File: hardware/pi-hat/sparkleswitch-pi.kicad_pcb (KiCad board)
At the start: 2 copper layers, 65 x 56 mm, 21 parts, among them J1 Conn_01x02, J2 Conn_02x06_Odd_Even, P1 CONN_02X20, U1 74HCT245, U2 74HCT245, U3 74HCT245, U4 PC817, U5 PC817, U6 PC817, U7 PC817

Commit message: First version with all connections.
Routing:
- net VCC: track 2.54 -> 118.8 mm, vias 0 -> 2
- net GND: track 82.3 -> 96.0 mm, vias 0 -> 6
- net Net-(R4-Pad2): track 0.00 -> 2.56 mm
- net Net-(R5-Pad1): track 0.00 -> 2.56 mm
- net Net-(R2-Pad2): track 0.00 -> 2.55 mm
- net Net-(R3-Pad2): track 0.00 -> 2.46 mm
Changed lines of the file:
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@@
     (thickness 1.6)
     (drawings 11)
-    (tracks 351)
+    (tracks 424)
     (zones 0)
     (modules 21)
@@
     (46 B.CrtYd user)
     (47 F.CrtYd user)
+    (48 B.Fab user)
+    (49 F.Fab user)
   )
   (setup
-    (last_trace_width 0.2)
+    (last_trace_width 0.5)
     (user_trace_width 0.5)
     (trace_clearance 0.2)
@@
   (segment (start 232.635 118.906) (end 232.635 119.206) (width 0.2) (layer F.Cu) (net 1))
   (segment (start 248.768 123.33) (end 248.768 120.79) (width 0.5) (layer B.Cu) (net 1))
-  (segment (start 248.768 113.272) (end 247.65 112.154) (width 0.5) (layer B.Cu) (net 1))
-  (segment (start 248.768 120.79) (end 248.768 113.272) (width 0.5) (layer B.Cu) (net 1))
   (segment (start 219.379999 97.920001) (end 218.53 98.77) (width 0.2) (layer F.Cu) (net 1))
   (segment (start 219.919999 97.380001) (end 219.379999 97.920001) (width 0.2) (layer F.Cu) (net 1))
   (segment (start 222.459999 97.380001) (end 219.919999 97.380001) (width 0.2) (layer F.Cu) (net 1))
   (segment (start 223.61 96.23) (end 222.459999 97.380001) (width 0.2) (layer F.Cu) (net 1))
+  (segment (start 232.635 118.906) (end 232.635 119.606) (width 0.2) (layer F.Cu) (net 1))
+  (segment (start 235.889 122.06) (end 235.889 122.06) (width 0.2) (layer F.Cu) (net 2))
+  (segment (start 221.205 118.906) (end 221.205 119.606) (width 0.2) (layer F.Cu) (net 1))
+  (segment (start 207.235 118.906) (end 207.235 119.606) (width 0.2) (layer F.Cu) (net 1))
+  (via (at 233.401 120.536) (size 0.9) (drill 0.6) (layers F.Cu B.Cu) (net 1))
+  (via (at 222.098 120.536) (size 0.9) (drill 0.6) (layers F.Cu B.Cu) (net 1))
+  (via (at 208.128 120.663) (size 0.9) (drill 0.6) (layers F.Cu B.Cu) (net 1))
+  (via (at 211.938 123.076) (size 0.9) (drill 0.6) (layers F.Cu B.Cu) (net 1))
+  (via (at 225.908 123.203) (size 0.9) (drill 0.6) (layers F.Cu B.Cu) (net 1))
+  (via (at 237.211 123.203) (size 0.9) (drill 0.6) (layers F.Cu B.Cu) (net 1))
+  (segment (start 232.635 119.77) (end 232.635 118.906) (width 0.2) (layer F.Cu) (net 1))
+  (segment (start 233.401 120.536) (end 232.635 119.77) (width 0.2) (layer F.Cu) (net 1))
+  (segment (start 237.835 123.827) (end 237.835 124.706) (width 0.2) (layer F.Cu) (net 1))
+  (segment (start 237.211 123.203) (end 237.835 123.827) (width 0.2) (layer F.Cu) (net 1))
+  (segment (start 226.405 123.573) (end 226.405 124.706) (width 0.2) (layer F.Cu) (net 1))
+  (segment (start 225.908 123.076) (end 226.405 123.573) (width 0.2) (layer F.Cu) (net 1))
+  (segment (start 221.205 119.643) (end 221.205 118.906) (width 0.2) (layer F.Cu) (net 1))
+  (segment (start 222.098 120.536) (end 221.205 119.643) (width 0.2) (layer F.Cu) (net 1))
+  (segment (start 207.235 119.77) (end 207.235 118.906) (width 0.2) (layer F.Cu) (net 1))
+  (segment (start 208.128 120.663) (end 207.235 119.77) (width 0.2) (layer F.Cu) (net 1))
+  (segment (start 212.435 123.573) (end 212.435 124.706) (width 0.2) (layer F.Cu) (net 1))
+  (segment (start 211.938 123.076) (end 212.435 123.573) (width 0.2) (layer F.Cu) (net 1))
+  (segment (start 247.65 113.28537) (end 247.625 113.31037) (width 0.5) (layer B.Cu) (net 1))
+  (segment (start 247.65 112.154) (end 247.65 113.28537) (width 0.5) (layer B.Cu) (net 1))
+  (segment (start 247.625 119.647) (end 248.768 120.79) (width 0.5) (layer B.Cu) (net 1))
+  (segment (start 247.625 113.31037) (end 247.625 119.647) (width 0.5) (layer B.Cu) (net 1))
   (segment (start 258.928 120.79) (end 258.928 123.33) (width 0.5) (layer B.Cu) (net 2))
+  (segment (start 238.485 118.906) (end 238.485 119.906) (width 0.5) (layer F.Cu) (net 2))
+  (segment (start 230.228 122.187) (end 227.055 122.187) (width 0.5) (layer F.Cu) (net 2))
+  (segment (start 230.24 122.175) (end 230.228 122.187) (width 0.5) (layer F.Cu) (net 2))
+  (segment (start 231.115 122.175) (end 230.24 122.175) (width 0.5) (layer F.Cu) (net 2))
+  (segment (start 227.055 118.906) (end 227.055 122.187) (width 0.5) (layer F.Cu) (net 2))
+  (segment (start 227.055 122.187) (end 227.055 124.706) (width 0.5) (layer F.Cu) (net 2))
+  (segment (start 231.115 122.175) (end 238.37 122.175) (width 0.5) (layer F.Cu) (net 2))
+  (segment (start 238.37 122.175) (end 238.485 122.06) (width 0.5) (layer F.Cu) (net 2))
+  (segment (start 220.179 122.175) (end 220.191 122.187) (width 0.5) (layer F.Cu) (net 2))
+  (segment (start 220.191 122.187) (end 227.055 122.187) (width 0.5) (layer F.Cu) (net 2))
+  (segment (start 219.304 122.175) (end 220.179 122.175) (width 0.5) (layer F.Cu) (net 2))
+  (segment (start 213.097 122.175) (end 213.085 122.187) (width 0.5) (layer F.Cu) (net 2))
+  (segment (start 219.304 122.175) (end 213.097 122.175) (width 0.5) (layer F.Cu) (net 2))
+  (segment (start 213.085 118.906) (end 213.085 122.187) (width 0.5) (layer F.Cu) (net 2))
+  (segment (start 213.085 122.187) (end 213.085 124.706) (width 0.5) (layer F.Cu) (net 2))
+  (segment (start 213.073 122.175) (end 205.334 122.175) (width 0.5) (layer F.Cu) (net 2))
+  (segment (start 213.085 122.187) (end 213.073 122.175) (width 0.5) (layer F.Cu) (net 2))
+  (segment (start 258.928 123.33) (end 257.15 125.108) (width 0.5) (layer B.Cu) (net 2))
+  (via (at 241.91 123.076) (size 0.9) (drill 0.6) (layers F.Cu B.Cu) (net 2))
+  (segment (start 257.15 125.108) (end 243.942 125.108) (width 0.5) (layer B.Cu) (net 2))
+  (segment (start 243.942 125.108) (end 241.91 123.076) (width 0.5) (layer B.Cu) (net 2))
+  (segment (start 241.460001 122.626001) (end 238.543001 122.626001) (width 0.5) (layer F.Cu) (net 2))
+  (segment (start 238.543001 122.626001) (end 238.485 122.568) (width 0.5) (layer F.Cu) (net 2))
+  (segment (start 238.485 122.06) (end 238.485 122.568) (width 0.5) (layer F.Cu) (net 2))
+  (segment (start 241.91 123.076) (end 241.460001 122.626001) (width 0.5) (layer F.Cu) (net 2))
+  (segment (start 238.485 122.568) (end 238.485 124.706) (width 0.5) (layer F.Cu) (net 2))
+  (via (at 241.91 121.552) (size 0.9) (drill 0.6) (layers F.Cu B.Cu) (net 2))
+  (segment (start 241.656 121.298) (end 241.91 121.552) (width 0.5) (layer F.Cu) (net 2))
+  (segment (start 238.485 119.906) (end 238.485 121.298) (width 0.5) (layer F.Cu) (net 2))
+  (segment (start 238.485 121.298) (end 241.656 121.298) (width 0.5) (layer F.Cu) (net 2))
+  (segment (start 238.485 121.298) (end 238.485 122.06) (width 0.5) (layer F.Cu) (net 2))
+  (segment (start 241.91 121.552) (end 241.91 123.076) (width 0.5) (layer B.Cu) (net 2))
+  (segment (start 203.937 100.663) (end 203.937 109.289) (width 0.5) (layer B.Cu) (net 2))
+  (segment (start 208.37 96.23) (end 203.937 100.663) (width 0.5) (layer B.Cu) (net 2))
+  (segment (start 210.91 96.23) (end 208.37 96.23) (width 0.5) (layer B.Cu) (net 2))
+  (segment (start 205.286 107.94) (end 203.937 109.289) (width 0.5) (layer F.Cu) (net 2))
+  (segment (start 205.286 105.042) (end 205.286 107.94) (width 0.5) (layer F.Cu) (net 2))
+  (segment (start 203.937 109.289) (end 202.159 111.067) (width 0.5) (layer F.Cu) (net 2))
+  (segment (start 202.159 111.067) (end 202.159 121.044) (width 0.5) (layer F.Cu) (net 2))
+  (segment (start 203.29 122.175) (end 205.334 122.175) (width 0.5) (layer F.Cu) (net 2))
+  (segment (start 202.159 121.044) (end 203.29 122.175) (width 0.5) (layer F.Cu) (net 2))
   (segment (start 207.288 98.77) (end 205.08 100.978) (width 0.5) (layer F.Cu) (net 3))
   (segment (start 208.37 98.77) (end 207.288 98.77) (width 0.5) (layer F.Cu) (net 3))
@@
   (segment (start 224.455 125.9886) (end 235.7664 137.3) (width 0.2) (layer F.Cu) (net 46))
   (segment (start 224.455 124.706) (end 224.455 125.9886) (width 0.2) (layer F.Cu) (net 46))
+  (segment (start 245.72 112.764) (end 245.11 112.154) (width 0.2) (layer F.Cu) (net 47))
+  (segment (start 245.72 114.452) (end 245.72 112.764) (width 0.2) (layer F.Cu) (net 47))
+  (segment (start 250.546 112.51) (end 250.19 112.154) (width 0.2) (layer F.Cu) (net 48))
+  (segment (start 250.546 114.464) (end 250.546 112.51) (width 0.2) (layer F.Cu) (net 48))
+  (segment (start 255.88 112.764) (end 255.27 112.154) (width 0.2) (layer F.Cu) (net 49))
+  (segment (start 255.88 114.464) (end 255.88 112.764) (width 0.2) (layer F.Cu) (net 49))
+  (segment (start 260.96 112.764) (end 260.35 112.154) (width 0.2) (layer F.Cu) (net 50))
+  (segment (start 260.96 114.464) (end 260.96 112.764) (width 0.2) (layer F.Cu) (net 50))
   (segment (start 246.47 115.952) (end 251.308 120.79) (width 0.2) (layer F.Cu) (net 51))
   (segment (start 245.72 115.952) (end 246.47 115.952) (width 0.2) (layer F.Cu) (net 51))

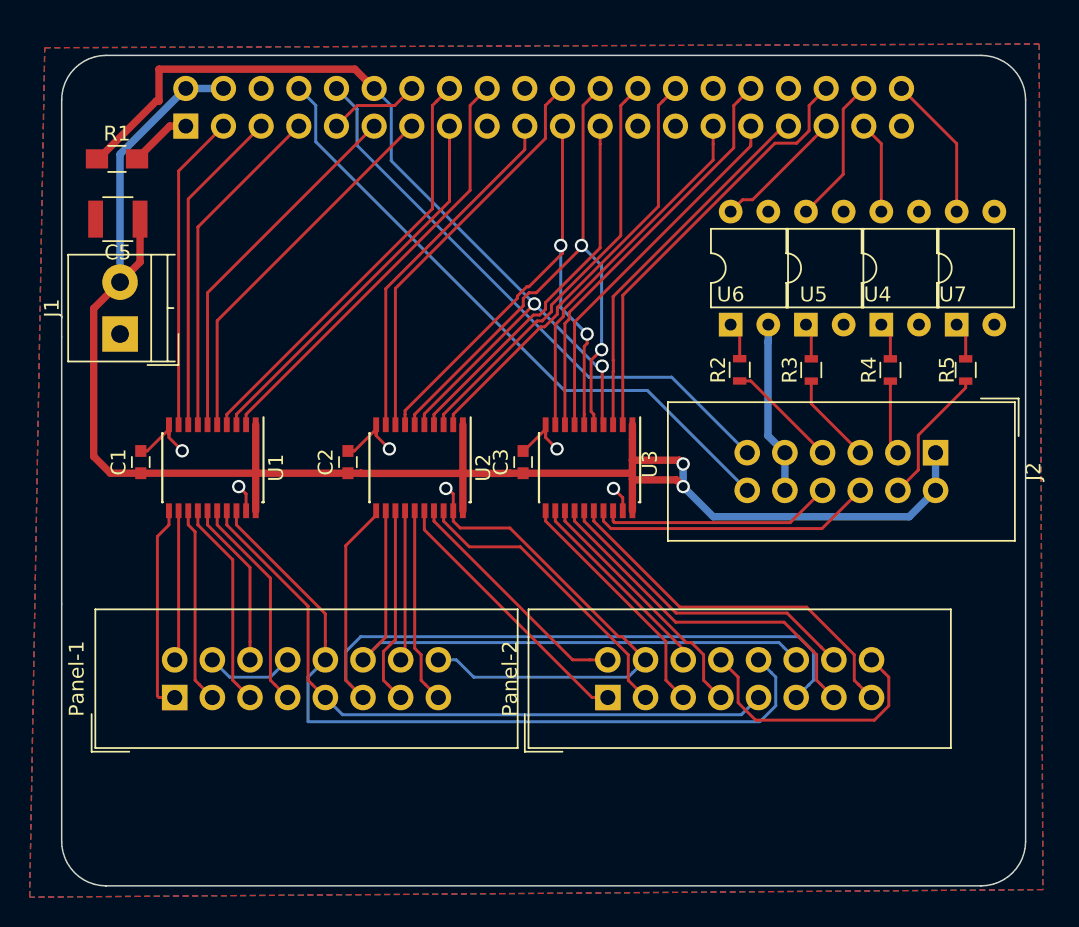
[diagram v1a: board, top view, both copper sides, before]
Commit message: Make traces thicker as we have the space.
o Increase size of traces from 0.25mm to 0.4mm as space is
  not that constricted (right now only the afferent traces).
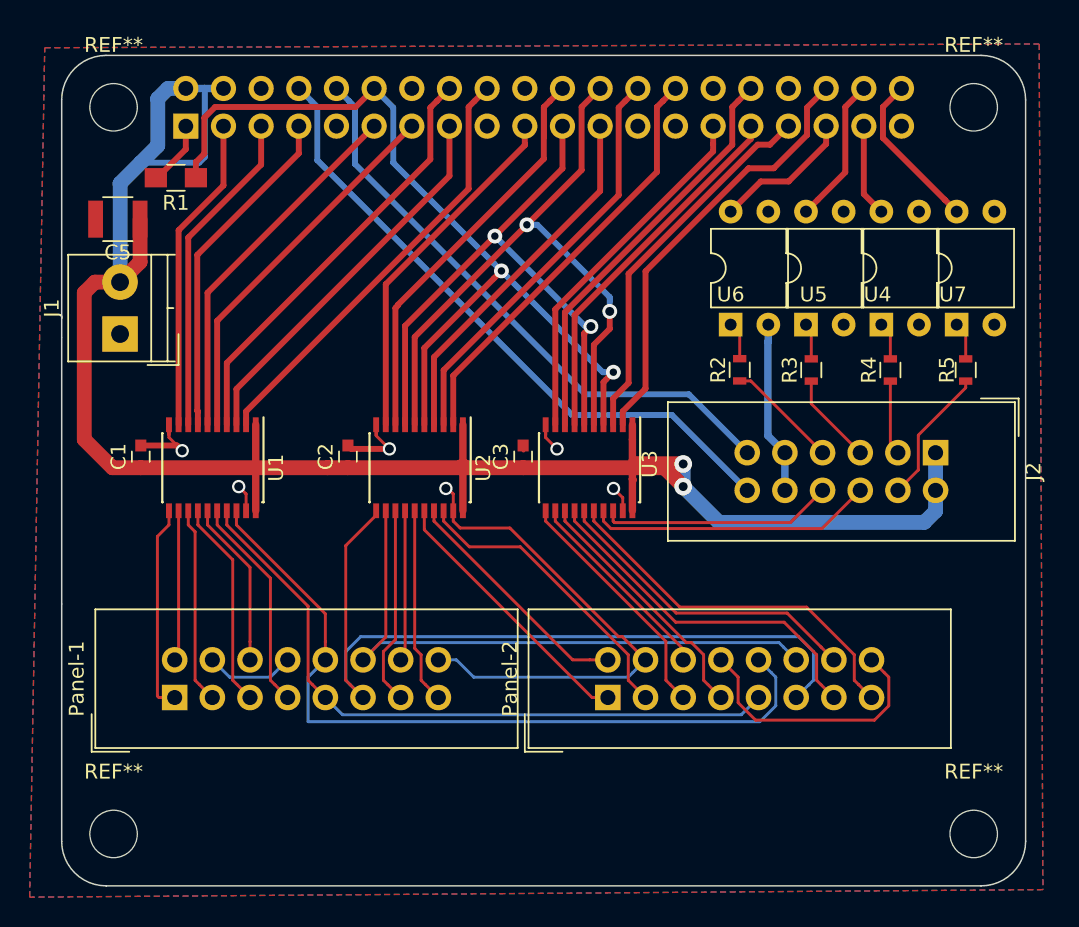
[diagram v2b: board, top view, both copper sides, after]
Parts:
- added REF**: M1, Mounting_Holes:MountingHole_3.2mm_M3, F.Cu at (203.5, 97.5)
- added REF**: M2, Mounting_Holes:MountingHole_3.2mm_M3, F.Cu at (261.5, 97.5)
- added REF**: M3, Mounting_Holes:MountingHole_3.2mm_M3, F.Cu at (261.5, 146.5)
- added REF**: M4, Mounting_Holes:MountingHole_3.2mm_M3, F.Cu at (203.5, 146.5)
- moved R1 4.17 mm to (207.7, 102.2), turned to 180 degrees
- moved C1 0.37 mm to (205.3, 121.1)
- moved C2 0.37 mm to (219.3, 121.1)
- moved C3 0.37 mm to (231.1, 121.1)
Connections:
- P1 pad 9: GND -> Net-(P1-Pad9)
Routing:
- net VCC: track 118.8 -> 135.5 mm
- net GND: track 96.0 -> 88.6 mm
- net OE: track 63.5 -> 60.0 mm
- net strobe: track 41.3 -> 44.5 mm
- net row_D: track 27.3 -> 30.0 mm
- net clock: track 38.1 -> 40.3 mm
- net SenseRelay: track 9.84 -> 10.9 mm
- net RxD: track 39.3 -> 40.1 mm
- net But-On: track 8.83 -> 9.53 mm
- net p0_b2: track 28.9 -> 29.6 mm
- net TxD: track 42.9 -> 43.6 mm
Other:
- net class Default: via_dia 0.9 -> 1

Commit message: Thicker efferent traces.
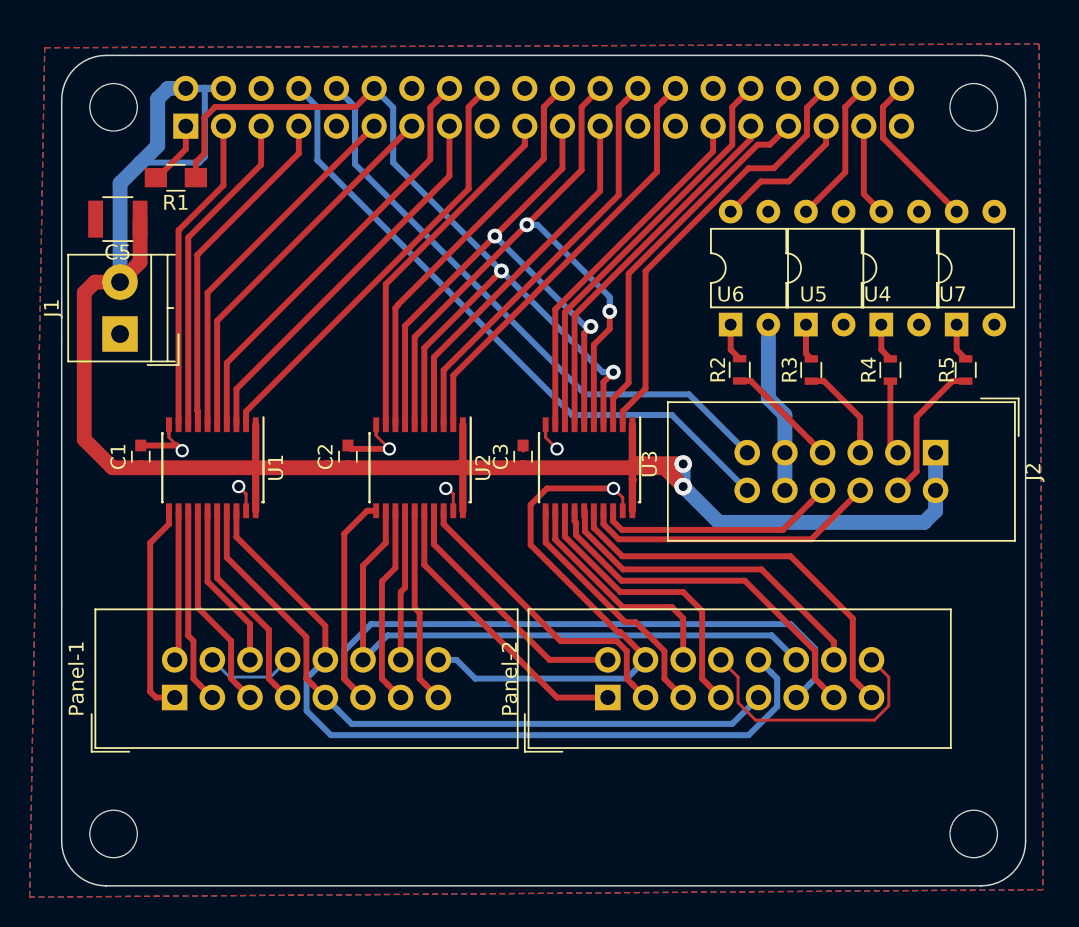
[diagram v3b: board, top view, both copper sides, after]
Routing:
- net GND: track 88.6 -> 90.9 mm
- net p1_b2_buff: track 17.2 -> 19.4 mm
- net p1_g2_buf: track 13.6 -> 15.6 mm
- net OE_buff_1: track 25.4 -> 27.0 mm
- net row_C_buff: track 53.5 -> 55.0 mm
- net p1_r1_buff: track 18.3 -> 19.7 mm
- net strobe_buff_1: track 21.4 -> 22.5 mm
- net p1_g1_buff: track 16.3 -> 17.2 mm
- net row_B_buff: track 52.5 -> 53.4 mm
- net Net-(R4-Pad2): track 2.56 -> 3.43 mm
- net Net-(R2-Pad2): track 2.55 -> 3.41 mm
- net Net-(R5-Pad1): track 2.56 -> 3.43 mm
- net p0_r1_buff: track 13.8 -> 14.5 mm
- net row_A_buff: track 45.3 -> 46.0 mm
- net RL-Trigger-Off_buff: track 19.3 -> 20.0 mm
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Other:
- net class Default: trace_width 0.2 -> 0.4; via_drill 0.6 -> 0.5

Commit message: More space between Led Matrix HUB75 IDC connectors.
.. to make sure they don't physically interfere.
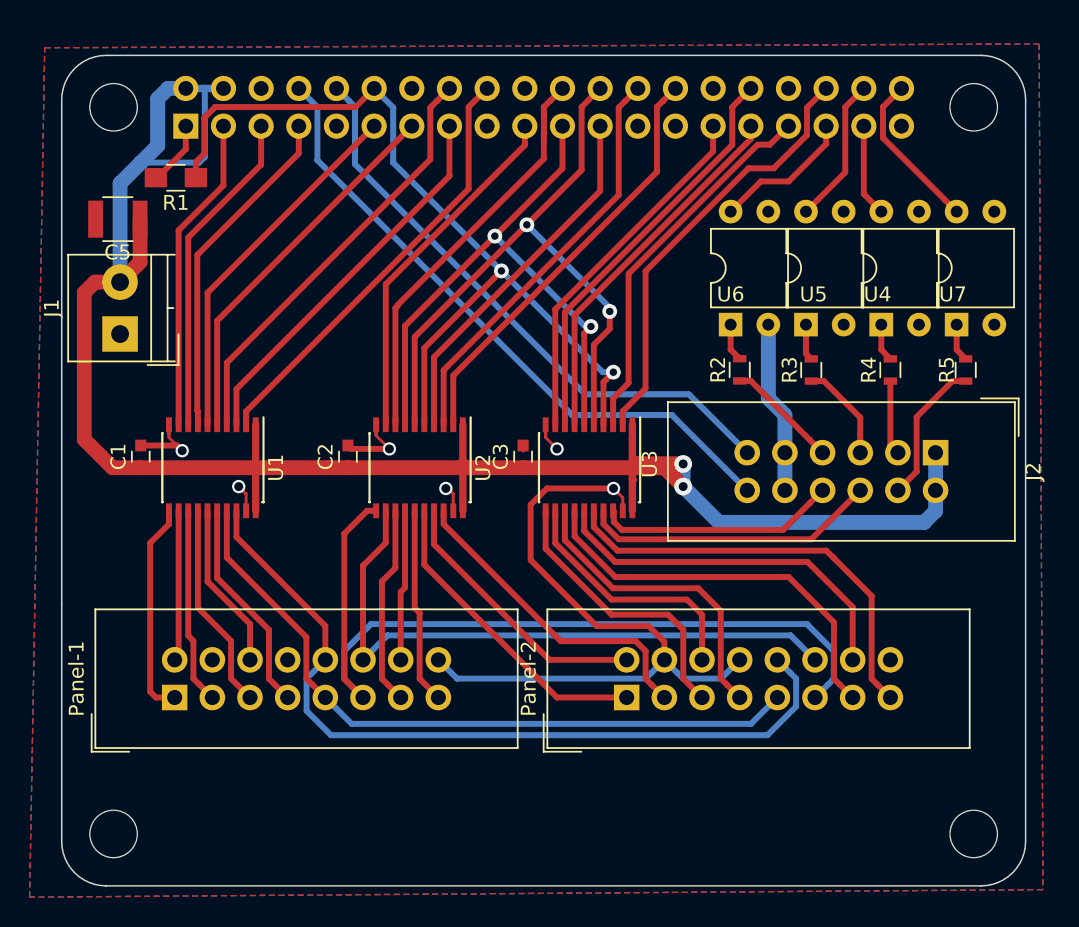
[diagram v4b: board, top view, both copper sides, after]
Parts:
- moved Panel-2 1.27 mm to (238.1, 137.3)
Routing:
- net GND: track 90.9 -> 76.7 mm
- net strobe_buff_1: track 22.5 -> 25.2 mm
- net clock_buff_1: track 24.7 -> 27.2 mm
- net p1_r2_buff: track 16.8 -> 19.2 mm
- net OE_buff_1: track 27.0 -> 29.3 mm
- net p1_g2_buf: track 15.6 -> 17.1 mm
- net p1_b2_buff: track 19.4 -> 20.8 mm
- net row_B_buff: track 53.4 -> 54.7 mm
- net row_D_buff: track 41.3 -> 42.5 mm
- net row_A_buff: track 46.0 -> 47.3 mm
- net p1_r1_buff: track 19.7 -> 21.0 mm
- net p1_g1_buff: track 17.2 -> 18.5 mm
- net p1_b1_buff: track 20.5 -> 21.7 mm
- net row_C_buff: track 55.0 -> 56.2 mm

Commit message: Center middle '245
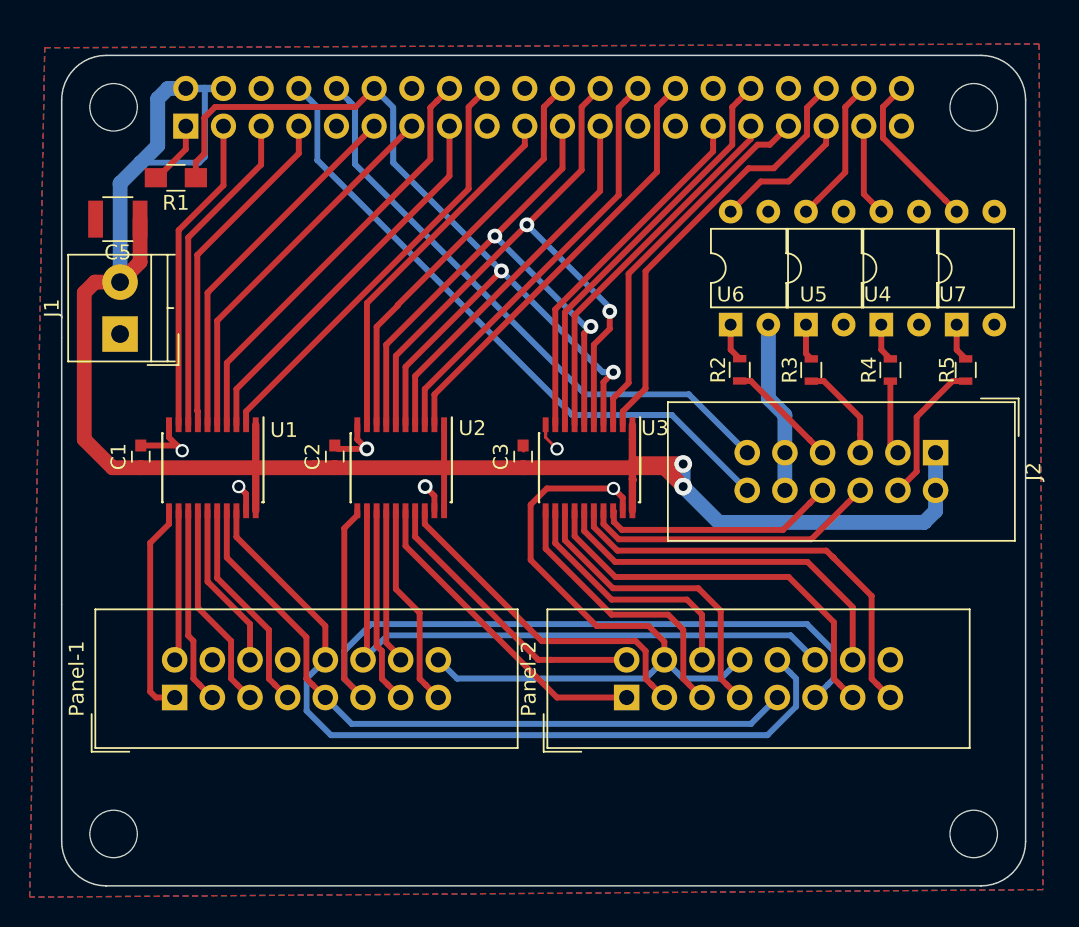
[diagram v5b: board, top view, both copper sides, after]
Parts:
- moved U2 1.27 mm to (222.9, 121.8)
- moved C2 0.89 mm to (218.4, 121.1)
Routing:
- net GND: track 76.7 -> 74.7 mm
- net p1_b1_buff: track 21.7 -> 23.0 mm
- net p1_g1_buff: track 18.5 -> 19.6 mm
- net row_C_buff: track 56.2 -> 55.3 mm
- net row_D: track 30.0 -> 30.8 mm
- net OE_buff_0: track 13.3 -> 13.8 mm
- net p1_r1_buff: track 21.0 -> 21.5 mm
- net p1_b1: track 28.9 -> 29.4 mm
- net strobe: track 44.1 -> 44.6 mm
- net clock: track 40.3 -> 40.9 mm
- net row_D_buff: track 42.5 -> 42.0 mm
- net row_C: track 24.0 -> 24.5 mm
- net p1_r1: track 24.8 -> 25.3 mm
- net p1_g1: track 28.1 -> 28.6 mm
